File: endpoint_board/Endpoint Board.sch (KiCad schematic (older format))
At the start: 11 parts, among them P1 POWER, P2 LIGHT, P3 ESP, P4 SERIAL, P5 RUN, P6 PGRM, SW1 Switch_SPDT_x2, U1 LM3671

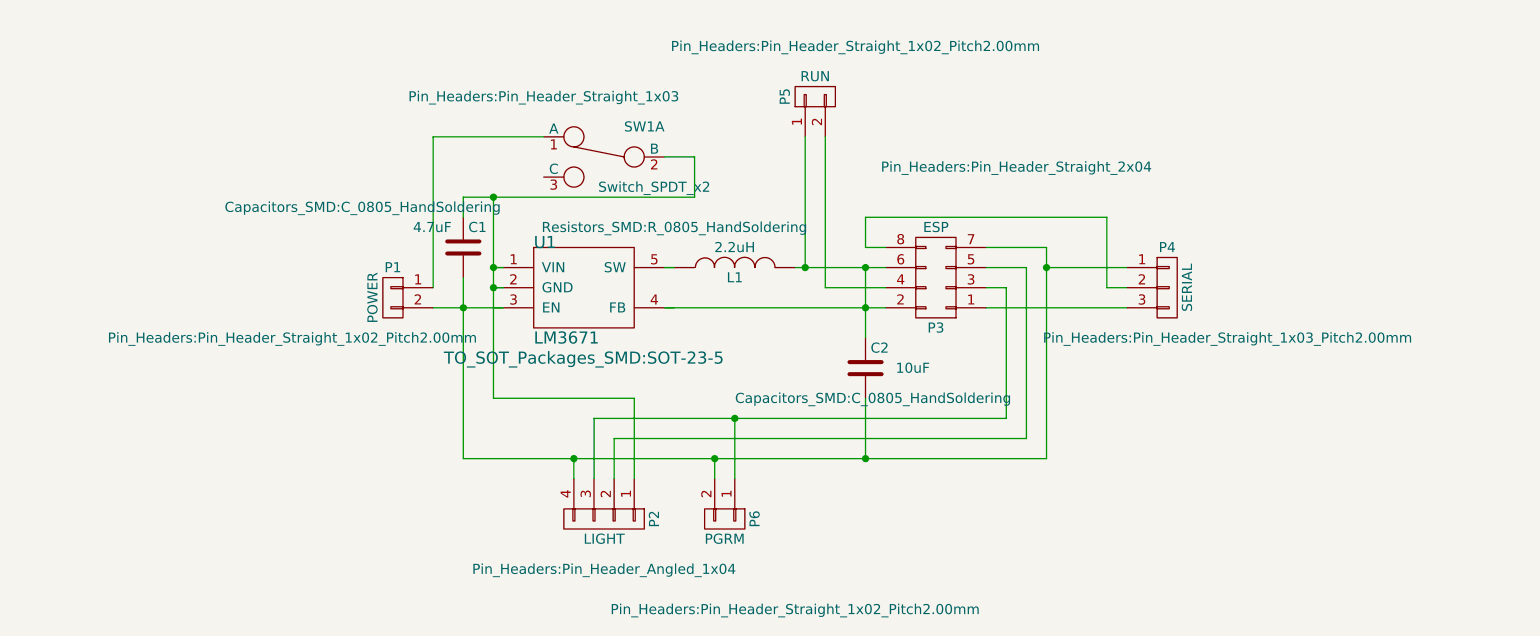
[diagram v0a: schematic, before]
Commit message: Cleaned up endpoint board to use newer submodule pattern
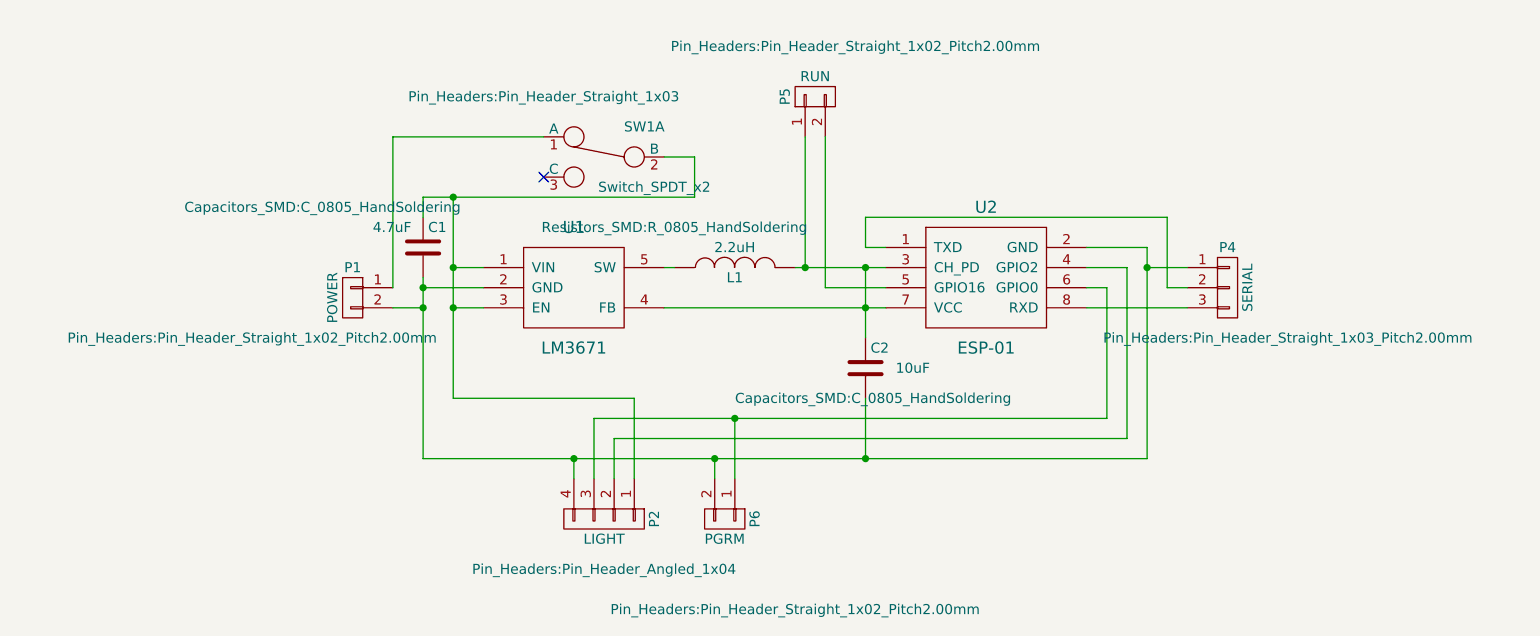
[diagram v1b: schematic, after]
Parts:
- removed P3: ESP, Pin_Headers:Pin_Header_Straight_2x04, symbol CONN_02X04
- added U2: ESP-01, symbol ESP-01
- U1: footprint TO_SOT_Packages_SMD:SOT-23-5 -> (none)
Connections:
- wire segments 42 -> 43
- no-connect marks 0 -> 1
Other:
- moved on the sheet: C1, P1, P4
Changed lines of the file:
@@
 LIBS:contrib
 LIBS:valves
-LIBS:lm3671
+LIBS:nebrius-microcontrollers
+LIBS:nebrius-regulators
 LIBS:Endpoint Board-cache
 EELAYER 25 0
@@
 $EndDescr
 $Comp
-L LM3671 U1
-U 1 1 57A0D83A
-P 6150 3750
-F 0 "U1" H 5900 3975 60  0000 L CNN
-F 1 "LM3671" H 5900 3500 60  0000 L CNN
-F 2 "TO_SOT_Packages_SMD:SOT-23-5" H 6150 3400 60  0000 C CNN
-F 3 "" H 6150 3400 60  0000 C CNN
-	1    6150 3750
-	1    0    0    -1
-$EndComp
-$Comp
 L Switch_SPDT_x2 SW1
 U 1 1 57A0DADD
@@
 L CONN_01X02 P1
 U 1 1 57A0DC23
-P 5200 3800
-F 0 "P1" H 5200 3950 50  0000 C CNN
-F 1 "POWER" V 5300 3800 50  0000 C CNN
-F 2 "Pin_Headers:Pin_Header_Straight_1x02_Pitch2.00mm" H 5700 3600 50  0000 C CNN
-F 3 "" H 5200 3800 50  0000 C CNN
-	1    5200 3800
+P 5000 3800
+F 0 "P1" H 5000 3950 50  0000 C CNN
+F 1 "POWER" V 5100 3800 50  0000 C CNN
+F 2 "Pin_Headers:Pin_Header_Straight_1x02_Pitch2.00mm" H 5500 3600 50  0000 C CNN
+F 3 "" H 5000 3800 50  0000 C CNN
+	1    5000 3800
 	-1   0    0    -1
 $EndComp
@@
 L C C1
 U 1 1 57A0E3BE
-P 5550 3550
-F 0 "C1" H 5575 3650 50  0000 L CNN
-F 1 "4.7uF" H 5300 3650 50  0000 L CNN
-F 2 "Capacitors_SMD:C_0805_HandSoldering" H 5050 3750 50  0000 C CNN
-F 3 "" H 5550 3550 50  0000 C CNN
-	1    5550 3550
+P 5350 3550
+F 0 "C1" H 5375 3650 50  0000 L CNN
+F 1 "4.7uF" H 5100 3650 50  0000 L CNN
+F 2 "Capacitors_SMD:C_0805_HandSoldering" H 4850 3750 50  0000 C CNN
+F 3 "" H 5350 3550 50  0000 C CNN
+	1    5350 3550
 	1    0    0    -1
 $EndComp
@@
 L CONN_01X03 P4
 U 1 1 584F7038
-P 9050 3750
-F 0 "P4" H 9050 3950 50  0000 C CNN
-F 1 "SERIAL" V 9150 3750 50  0000 C CNN
-F 2 "Pin_Headers:Pin_Header_Straight_1x03_Pitch2.00mm" H 9350 3500 50  0000 C CNN
-F 3 "" H 9050 3750 50  0000 C CNN
-	1    9050 3750
-	1    0    0    -1
-$EndComp
-$Comp
-L CONN_02X04 P3
-U 1 1 5850C0A1
-P 7900 3700
-F 0 "P3" H 7900 3950 50  0000 C CNN
-F 1 "ESP" H 7900 3450 50  0000 C CNN
-F 2 "Pin_Headers:Pin_Header_Straight_2x04" H 7500 3150 50  0000 C CNN
-F 3 "" H 7900 2500 50  0000 C CNN
-	1    7900 3700
-	-1   0    0    1
-$EndComp
-Wire Wire Line
-	5400 3750 5400 3000
-Wire Wire Line
-	5400 3000 5950 3000
+P 9350 3750
+F 0 "P4" H 9350 3950 50  0000 C CNN
+F 1 "SERIAL" V 9450 3750 50  0000 C CNN
+F 2 "Pin_Headers:Pin_Header_Straight_1x03_Pitch2.00mm" H 9650 3500 50  0000 C CNN
+F 3 "" H 9350 3750 50  0000 C CNN
+	1    9350 3750
+	1    0    0    -1
+$EndComp
+Wire Wire Line
+	5200 3750 5200 3000
+Wire Wire Line
+	5200 3000 5950 3000
 Wire Wire Line
 	6550 3100 6700 3100
 Wire Wire Line
-	5700 3300 5700 4300
-Wire Wire Line
-	5700 3650 5750 3650
-Wire Wire Line
-	5700 4300 6400 4300
-Connection ~ 5700 3650
-Wire Wire Line
-	5400 3850 5750 3850
-Wire Wire Line
-	5550 3700 5550 4600
-Wire Wire Line
-	5550 4600 8450 4600
-Connection ~ 5550 3850
+	5500 3300 5500 4300
+Wire Wire Line
+	5500 4300 6400 4300
+Wire Wire Line
+	5350 3850 5200 3850
+Wire Wire Line
+	5350 3700 5350 4600
+Wire Wire Line
+	8950 4600 5350 4600
+Connection ~ 5350 3850
 Wire Wire Line
 	6550 3650 6600 3650
 Wire Wire Line
-	6700 3100 6700 3300
-Wire Wire Line
-	6700 3300 5550 3300
-Wire Wire Line
-	5550 3300 5550 3400
-Connection ~ 5700 3300
+	6700 3300 6700 3100
+Wire Wire Line
+	5350 3300 6700 3300
+Wire Wire Line
+	5350 3300 5350 3400
+Connection ~ 5500 3300
 Wire Wire Line
 	7550 3650 7550 4000
@@
 	7550 4600 7550 4300
 Wire Wire Line
-	5750 3750 5700 3750
-Connection ~ 5700 3750
-Wire Wire Line
 	7200 3650 7650 3650
 Wire Wire Line
-	8150 3550 8450 3550
-Wire Wire Line
-	8450 3550 8450 4600
+	8650 3550 8950 3550
+Wire Wire Line
+	8950 3550 8950 4600
 Connection ~ 7550 4600
 Wire Wire Line
-	8250 3750 8250 4400
-Wire Wire Line
-	8250 3750 8150 3750
-Wire Wire Line
-	8250 4400 6200 4400
+	8750 4400 8750 3750
+Wire Wire Line
+	8750 3750 8650 3750
+Wire Wire Line
+	6200 4400 8750 4400
 Wire Wire Line
 	6200 4400 6200 4700
 Wire Wire Line
-	8150 3650 8350 3650
-Wire Wire Line
-	8350 3650 8350 4500
-Wire Wire Line
-	8350 4500 6300 4500
+	8650 3650 8850 3650
+Wire Wire Line
+	8850 3650 8850 4500
+Wire Wire Line
+	8850 4500 6300 4500
 Wire Wire Line
 	6300 4500 6300 4700
 Connection ~ 7550 3650
 Wire Wire Line
-	8150 3850 8850 3850
+	8650 3850 9150 3850
 Wire Wire Line
 	7650 3550 7550 3550
@@
 	7550 3550 7550 3400
 Wire Wire Line
-	7550 3400 8750 3400
-Wire Wire Line
-	8750 3400 8750 3750
-Wire Wire Line
-	8750 3750 8850 3750
-Wire Wire Line
-	8850 3650 8450 3650
-Connection ~ 8450 3650
+	7550 3400 9050 3400
+Wire Wire Line
+	9050 3400 9050 3750
+Wire Wire Line
+	9050 3750 9150 3750
+Wire Wire Line
+	9150 3650 8950 3650
+Connection ~ 8950 3650
 Wire Wire Line
 	7650 3750 7350 3750
@@
 	6900 4700 6900 4400
 Connection ~ 6900 4400
+$Comp
+L LM3671 U1
+U 1 1 5AB1453B
+P 6100 3750
+F 0 "U1" H 6100 4050 60  0000 C CNN
+F 1 "LM3671" H 6100 3450 60  0000 C CNN
+F 2 "" H 6100 3750 60  0001 C CNN
+F 3 "" H 6100 3750 60  0001 C CNN
+	1    6100 3750
+	1    0    0    -1
+$EndComp
+Wire Wire Line
+	5650 3650 5500 3650
+Connection ~ 5500 3650
+Wire Wire Line
+	5650 3850 5500 3850
+Connection ~ 5500 3850
+Wire Wire Line
+	5650 3750 5350 3750
+Connection ~ 5350 3750
+$Comp
+L ESP-01 U2
+U 1 1 5AB148BB
+P 8150 3700
+F 0 "U2" H 8150 4050 60  0000 C CNN
+F 1 "ESP-01" H 8150 3350 60  0000 C CNN
+F 2 "" H 8150 3700 60  0001 C CNN
+F 3 "" H 8150 3700 60  0001 C CNN
+	1    8150 3700
+	1    0    0    -1
+$EndComp
+NoConn ~ 5950 3200
 $EndSCHEMATC

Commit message: Updated components
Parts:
- removed P2: LIGHT, Pin_Headers:Pin_Header_Angled_1x04, symbol CONN_01X04
- added U3: DotStar, symbol DotStar
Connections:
- net at C1.1, SW1.2 (B), U1.1 (VIN)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: now also U3.1 (VCC)
- net at C1.2, C2.2, P1.2 (P2)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: now also U3.4 (GND)
- net at U2.4 (GPIO2): now also U3.2 (CLK)
- net at P6.1 (P1), U2.6 (GPIO0): now also U3.3 (DATA)
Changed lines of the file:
@@
 EESchema Schematic File Version 2
+LIBS:diode
 LIBS:power
 LIBS:device
@@
 LIBS:nebrius-microcontrollers
 LIBS:nebrius-regulators
+LIBS:nebrius-lcd
 LIBS:Endpoint Board-cache
 EELAYER 25 0
@@
 $EndComp
 $Comp
-L CONN_01X04 P2
-U 1 1 57A0DCA2
-P 6250 4900
-F 0 "P2" H 6250 5150 50  0000 C CNN
-F 1 "LIGHT" V 6350 4900 50  0000 C CNN
-F 2 "Pin_Headers:Pin_Header_Angled_1x04" V 6500 4900 50  0000 C CNN
-F 3 "" H 6250 4900 50  0000 C CNN
-	1    6250 4900
-	0    1    1    0
-$EndComp
-$Comp
 L INDUCTOR L1
 U 1 1 57A0E1B1
@@
 F 0 "P6" H 6850 5050 50  0000 C CNN
 F 1 "PGRM" V 6950 4900 50  0000 C CNN
-F 2 "Pin_Headers:Pin_Header_Straight_1x02_Pitch2.00mm" V 7300 5250 50  0000 C CNN
+F 2 "Pin_Headers:Pin_Header_Straight_1x02_Pitch2.00mm" V 7150 5750 50  0000 C CNN
 F 3 "" H 6850 4900 50  0000 C CNN
 	1    6850 4900
@@
 $EndComp
 NoConn ~ 5950 3200
+$Comp
+L DotStar U3
+U 1 1 5AB151BC
+P 6250 5050
+F 0 "U3" H 6600 5100 60  0000 C CNN
+F 1 "DotStar" H 6250 5200 60  0000 C CNN
+F 2 "" H 6250 5050 60  0001 C CNN
+F 3 "" H 6250 5050 60  0001 C CNN
+	1    6250 5050
+	-1   0    0    1
+$EndComp
 $EndSCHEMATC

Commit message: First draft of the new receivers
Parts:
- removed P1: POWER, Pin_Headers:Pin_Header_Straight_1x02_Pitch2.00mm, symbol CONN_01X02
- removed P5: RUN, Pin_Headers:Pin_Header_Straight_1x02_Pitch2.00mm, symbol CONN_01X02
- removed P6: PGRM, Pin_Headers:Pin_Header_Straight_1x02_Pitch2.00mm, symbol CONN_01X02
- removed SW1: Switch_SPDT_x2, Pin_Headers:Pin_Header_Straight_1x03, symbol Switch_SPDT_x2
- removed U3: DotStar, symbol DotStar
- added R1, R3: 10k, Resistors_SMD:R_0805_HandSoldering, symbol R
- added R2: 1k, Resistors_SMD:R_0805_HandSoldering, symbol R
- added SW1: SW_DPST, nebrius-switch:KMR641NG, symbol SW_DPST
- added U3: NeoPixel, Pin_Headers:Pin_Header_Angled_1x03_Pitch2.54mm, symbol NeoPixel
- added U4: SN74LVC1T45, TO_SOT_Packages_SMD:TSOT-23-6_HandSoldering, symbol SN74LVC1T45
- U1: footprint (none) -> TO_SOT_Packages_SMD:SOT-23-5_HandSoldering
- U2: footprint (none) -> Pin_Headers:Pin_Header_Straight_2x04_Pitch2.54mm
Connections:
- net +5V: now reaches C1.1, U1.1 (VIN), U1.3 (EN)
- net +5V: now also U3.3 (VCC), U4.1 (VCCA)
- net GND: now reaches C1.2, C2.2, P4.1 (P1), U1.2 (GND), U2.2 (GND)
- net GND: now also SW1.2, U3.1 (GND), U4.2 (GND), U4.5 (DIR)
- net VCC: now reaches C2.1, L1.2, U1.4 (FB), U2.3 (CH_PD), U2.7 (VCC)
- net VCC: now also R1.1, R2.1, R3.1, U4.6 (VCCB)
- net at U2.5 (GPIO16): now also R1.2
- net at U2.6 (GPIO0): now also R2.2, SW1.1
- net at U2.4 (GPIO2): now also R3.2, U4.4 (B)
- new net: U3.2 (Data), U4.3 (A)
- no-connect marks 1 -> 2
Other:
- moved on the sheet: C1, C2, L1, U1
